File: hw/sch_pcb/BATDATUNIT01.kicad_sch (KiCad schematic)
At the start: 115 parts, among them IC1 MAX14502AETL+, J1 USBC_USB4105-GF-A, J22 HEADER_2x03, J4 46436-9327, J9 SD_Card-FPS009-4200-0, Q1 BC817-25, Q2 BC817-25, Q3 BC817-25, Q4 BC817-25, SW3 KMT031, SW3 SKRTLAE010, SW4 KMT031, SW4 SKRTLAE010, U10 ATMEGA1284P-AU, U11 PCF85263A, U11 TCA4307, U2 USBLC6-2SC6, U3 FT260Q-T, U4 PCA9541ABS/01, U6 AT24CS64-SSHM, U6 SHT35-DIS, U7 TMUX1574DYYR, Y1 19.2 MHz, Y1 8 MHz, Y2 ABS07-120-32.768KHZ-T

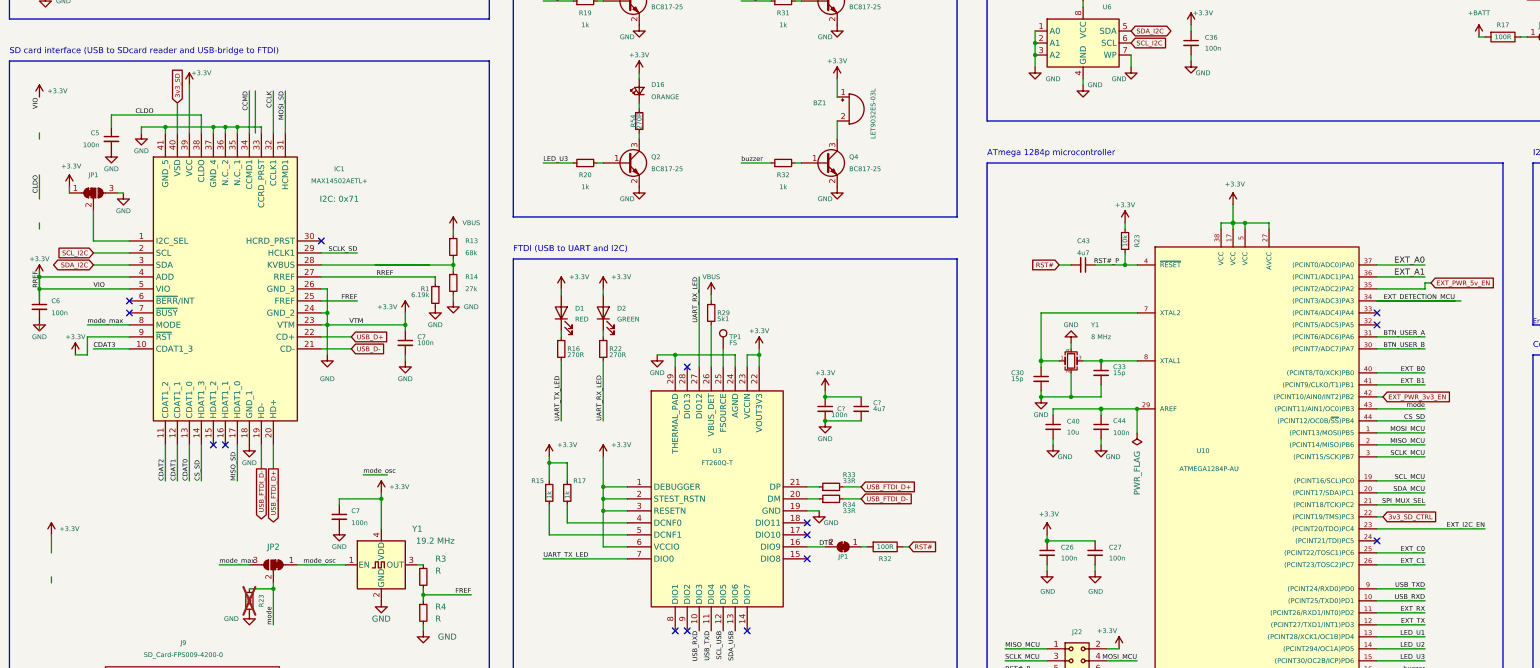
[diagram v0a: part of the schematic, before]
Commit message: Delete of unconnected wires after manual merge.
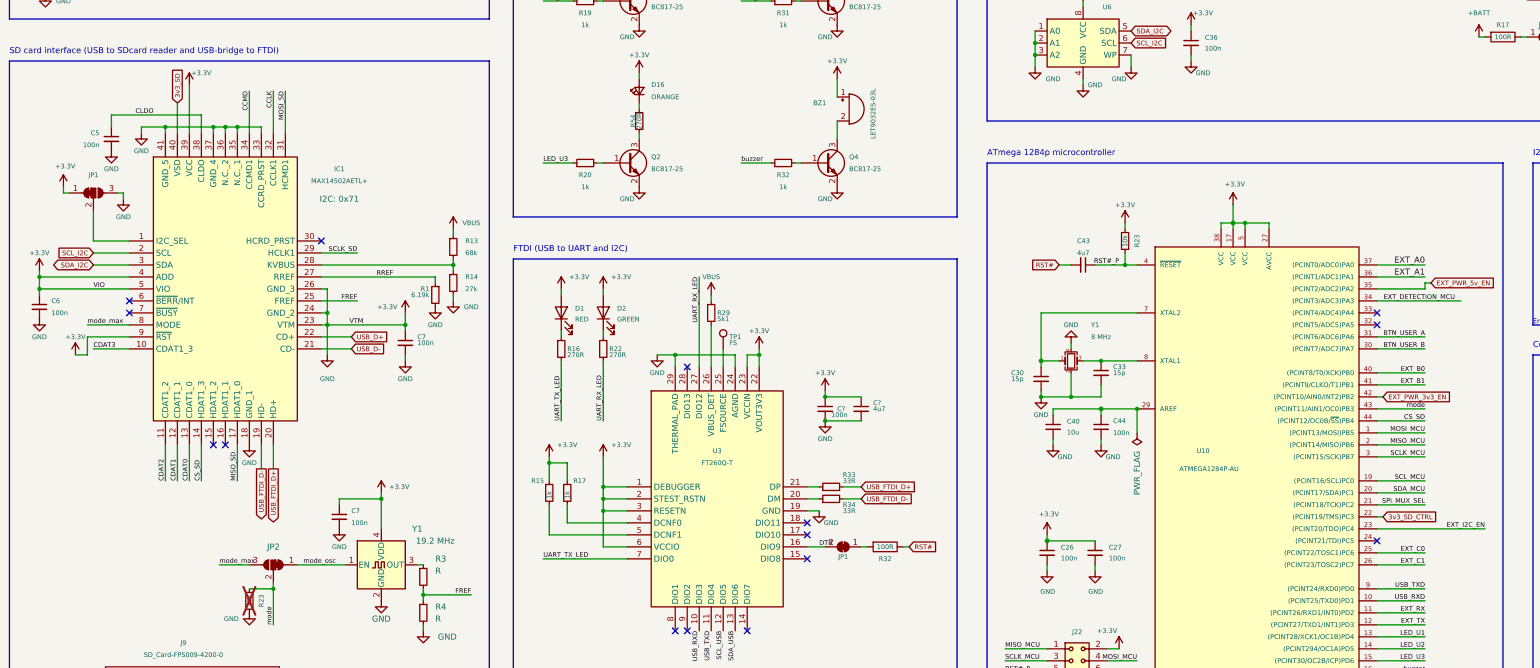
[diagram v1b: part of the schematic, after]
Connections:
- net +3.3V: no longer IC1.27 (RREF), R1.1
- new net RREF: IC1.27 (RREF), R1.1
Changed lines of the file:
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@@
     (stroke (width 0) (type default))
   )
-  (wire (pts (xy 21.59 106.68) (xy 21.59 111.76))
-    (stroke (width 0) (type default))
-  )
   (wire (pts (xy 190.5 57.15) (xy 190.5 58.42))
     (stroke (width 0) (type default))
@@
     (stroke (width 0) (type default))
   )
-  (wire (pts (xy 21.59 139.7) (xy 21.59 138.43))
-    (stroke (width 0) (type default))
-  )
   (wire (pts (xy 71.12 48.26) (xy 72.39 48.26))
     (stroke (width 0) (type default))
@@
     (stroke (width 0) (type default))
   )
-  (wire (pts (xy 21.59 97.79) (xy 21.59 99.06))
-    (stroke (width 0) (type default))
-  )
   (wire (pts (xy 173.99 144.78) (xy 173.99 147.32))
     (stroke (width 0) (type default))
@@
     (stroke (width 0) (type default))
   )
-  (wire (pts (xy 92.71 125.73) (xy 104.14 125.73))
+  (wire (pts (xy 81.28 125.73) (xy 109.22 125.73))
     (stroke (width 0) (type default))
   )
@@
     (stroke (width 0) (type default))
   )
-  (wire (pts (xy 90.17 170.18) (xy 95.25 170.18))
-    (stroke (width 0) (type default))
-  )
   (wire (pts (xy 74.93 218.44) (xy 76.2 218.44))
     (stroke (width 0) (type default))
@@
     (stroke (width 0) (type default))
   )
-  (wire (pts (xy 24.13 182.88) (xy 24.13 186.69))
-    (stroke (width 0) (type default))
-  )
   (wire (pts (xy 194.31 251.46) (xy 191.77 251.46))
     (stroke (width 0) (type default))
@@
     (stroke (width 0) (type default))
   )
+  (wire (pts (xy 39.37 110.49) (xy 39.37 111.76))
+    (stroke (width 0) (type default))
+  )
   (wire (pts (xy 368.3 210.82) (xy 368.3 201.93))
     (stroke (width 0) (type default))
@@
     (stroke (width 0) (type default))
   )
-  (wire (pts (xy 21.59 127) (xy 21.59 133.35))
+  (wire (pts (xy 21.59 127) (xy 21.59 128.27))
     (stroke (width 0) (type default))
   )
@@
     (stroke (width 0) (type default))
   )
-  (wire (pts (xy 304.8 133.35) (xy 321.31 133.35))
-    (stroke (width 0) (type default))
-  )
   (wire (pts (xy 359.41 38.1) (xy 359.41 39.37))
     (stroke (width 0) (type default))
@@
     (stroke (width 0) (type default))
   )
+  (wire (pts (xy 26.67 110.49) (xy 27.94 110.49))
+    (stroke (width 0) (type default))
+  )
   (wire (pts (xy 53.34 163.83) (xy 53.34 171.45))
     (stroke (width 0) (type default))
@@
     (stroke (width 0) (type default))
   )
-  (wire (pts (xy 67.31 88.9) (xy 67.31 97.79))
-    (stroke (width 0) (type default))
-  )
   (wire (pts (xy 232.41 52.07) (xy 233.68 52.07))
     (stroke (width 0) (type default))
@@
     (stroke (width 0) (type solid))
   )
-  (wire (pts (xy 24.13 193.04) (xy 24.13 191.77))
-    (stroke (width 0) (type default))
-  )
   (wire (pts (xy 77.47 228.6) (xy 74.93 228.6))
     (stroke (width 0) (type default))
@@
     (stroke (width 0) (type default))
   )
-  (wire (pts (xy 27.94 109.22) (xy 27.94 110.49))
+  (wire (pts (xy 26.67 109.22) (xy 26.67 110.49))
     (stroke (width 0) (type default))
   )
@@
     (stroke (width 0) (type default))
   )
-  (wire (pts (xy 21.59 118.11) (xy 21.59 116.84))
-    (stroke (width 0) (type default))
-  )
   (wire (pts (xy 284.48 52.07) (xy 285.75 52.07))
     (stroke (width 0) (type default))
@@
     (stroke (width 0) (type solid))
   )
-  (wire (pts (xy 81.28 125.73) (xy 109.22 125.73))
-    (stroke (width 0) (type default))
-  )
   (wire (pts (xy 95.25 213.36) (xy 85.09 213.36))
     (stroke (width 0) (type default))
@@
     (effects (font (size 1 1)) (justify left bottom))
   )
-  (label "CLDO" (at 21.59 106.68 270) (fields_autoplaced)
-    (effects (font (size 1 1)) (justify right bottom))
-  )
-  (label "RREF" (at 21.59 127 270) (fields_autoplaced)
-    (effects (font (size 1 1)) (justify right bottom))
-  )
   (label "EXT_A0" (at 314.96 125.73 180) (fields_autoplaced)
     (effects (font (size 1.27 1.27)) (justify right bottom))
@@
     (effects (font (size 1 1)) (justify right bottom))
   )
-  (label "VIO" (at 21.59 92.71 90) (fields_autoplaced)
-    (effects (font (size 1 1)) (justify left bottom))
-  )
   (label "CDAT2" (at 95.25 233.68 180) (fields_autoplaced)
     (effects (font (size 1 1)) (justify right bottom))
@@
     (effects (font (size 1 1)) (justify left bottom))
   )
-  (label "mode_osc" (at 90.17 170.18 0) (fields_autoplaced)
-    (effects (font (size 1 1)) (justify left bottom))
-  )
   (label "EXT_B1" (at 378.46 210.82 90) (fields_autoplaced)
     (effects (font (size 1 1)) (justify left bottom))
@@
     )
   )
-  (symbol (lib_id "power:+3.3V") (at 27.94 109.22 0) (unit 1)
+  (symbol (lib_id "power:+3.3V") (at 26.67 109.22 0) (unit 1)
     (in_bom yes) (on_board yes) (dnp no)
-    (property "Reference" "#PWR0135" (at 27.94 113.03 0)
+    (property "Reference" "#PWR0135" (at 26.67 113.03 0)
       (effects (font (size 1 1)) hide)
     )
-    (property "Value" "+3.3V" (at 28.321 104.8258 0)
+    (property "Value" "+3.3V" (at 27.051 104.8258 0)
       (effects (font (size 1 1)))
     )
-    (property "Footprint" "" (at 27.94 109.22 0)
+    (property "Footprint" "" (at 26.67 109.22 0)
       (effects (font (size 1 1)) hide)
     )
-    (property "Datasheet" "" (at 27.94 109.22 0)
+    (property "Datasheet" "" (at 26.67 109.22 0)
       (effects (font (size 1 1)) hide)
     )
@@
     )
   )
-  (symbol (lib_id "power:+3.3V") (at 24.13 182.88 0) (unit 1)
-    (in_bom yes) (on_board yes) (dnp no)
-    (property "Reference" "#PWR0135" (at 24.13 186.69 0)
-      (effects (font (size 1 1)) hide)
-    )
-    (property "Value" "+3.3V" (at 27.94 181.61 0)
-      (effects (font (size 1 1)))
-    )
-    (property "Footprint" "" (at 24.13 182.88 0)
-      (effects (font (size 1 1)) hide)
-    )
-    (property "Datasheet" "" (at 24.13 182.88 0)
-      (effects (font (size 1 1)) hide)
-    )
-    (pin "1")
-    (instances
-      (project "USTSIPIN02A"
-        (path "/0a87ced0-2af2-43c5-a56c-218f7013d76f/00000000-0000-0000-0000-00005c4aedd8"
-          (reference "#PWR0135") (unit 1)
-        )
-      )
-      (project "cpu"
-        (path "/4af4b710-5b7c-4fa3-ad36-3ed9c7e42fc3"
-          (reference "#PWR0135") (unit 1)
-        )
-      )
-      (project "BATDATUNIT01"
-        (path "/cca3030a-cb35-4155-89c2-3a41e5a0afad"
-          (reference "#PWR08") (unit 1)
-        )
-      )
-    )
-  )
   (symbol (lib_name "GND_2") (lib_id "power:GND") (at 152.4 144.78 0) (unit 1)
     (in_bom yes) (on_board yes) (dnp no)
@@
     )
   )
-  (symbol (lib_id "power:+3.3V") (at 21.59 128.27 0) (unit 1)
+  (symbol (lib_id "power:+3.3V") (at 21.59 127 0) (unit 1)
     (in_bom yes) (on_board yes) (dnp no)
-    (property "Reference" "#PWR0135" (at 21.59 132.08 0)
+    (property "Reference" "#PWR0135" (at 21.59 130.81 0)
       (effects (font (size 1 1)) hide)
     )
-    (property "Value" "+3.3V" (at 21.59 124.46 0)
+    (property "Value" "+3.3V" (at 21.59 123.19 0)
       (effects (font (size 1 1)))
     )
-    (property "Footprint" "" (at 21.59 128.27 0)
+    (property "Footprint" "" (at 21.59 127 0)
       (effects (font (size 1 1)) hide)
     )
-    (property "Datasheet" "" (at 21.59 128.27 0)
+    (property "Datasheet" "" (at 21.59 127 0)
       (effects (font (size 1 1)) hide)
     )
@@
     )
   )
-  (symbol (lib_id "power:+3.3V") (at 21.59 90.17 0) (unit 1)
-    (in_bom yes) (on_board yes) (dnp no)
-    (property "Reference" "#PWR0135" (at 21.59 93.98 0)
-      (effects (font (size 1 1)) hide)
-    )
-    (property "Value" "+3.3V" (at 25.4 88.9 0)
-      (effects (font (size 1 1)))
-    )
-    (property "Footprint" "" (at 21.59 90.17 0)
-      (effects (font (size 1 1)) hide)
-    )
-    (property "Datasheet" "" (at 21.59 90.17 0)
-      (effects (font (size 1 1)) hide)
-    )
-    (pin "1")
-    (instances
-      (project "USTSIPIN02A"
-        (path "/0a87ced0-2af2-43c5-a56c-218f7013d76f/00000000-0000-0000-0000-00005c4aedd8"
-          (reference "#PWR0135") (unit 1)
-        )
-      )
-      (project "cpu"
-        (path "/4af4b710-5b7c-4fa3-ad36-3ed9c7e42fc3"
-          (reference "#PWR0135") (unit 1)
-        )
-      )
-      (project "BATDATUNIT01"
-        (path "/cca3030a-cb35-4155-89c2-3a41e5a0afad"
-          (reference "#PWR01") (unit 1)
-        )
-      )
-    )
-  )
   (symbol (lib_id "power:GND") (at 177.8 39.37 0) (mirror y) (unit 1)
     (in_bom yes) (on_board yes) (dnp no)
@@
     )
   )
-  (symbol (lib_name "GND_1") (lib_id "power:GND") (at 39.37 110.49 0) (unit 1)
+  (symbol (lib_name "GND_1") (lib_id "power:GND") (at 39.37 111.76 0) (unit 1)
     (in_bom yes) (on_board yes) (dnp no)
-    (property "Reference" "#PWR06" (at 39.37 116.84 0)
+    (property "Reference" "#PWR06" (at 39.37 118.11 0)
       (effects (font (size 1 1)) hide)
     )
-    (property "Value" "GND" (at 39.37 114.3 0)
+    (property "Value" "GND" (at 39.37 115.57 0)
       (effects (font (size 1 1)))
     )
-    (property "Footprint" "" (at 39.37 110.49 0)
+    (property "Footprint" "" (at 39.37 111.76 0)
       (effects (font (size 1 1)) hide)
     )
-    (property "Datasheet" "" (at 39.37 110.49 0)
+    (property "Datasheet" "" (at 39.37 111.76 0)
       (effects (font (size 1 1)) hide)
     )
